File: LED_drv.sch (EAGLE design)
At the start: 46 parts, among them IC1 LM3409, IC2 LM393D, T1 IRLR9343PBF, T4 BT169, T5 BT169, T6 TLP266J

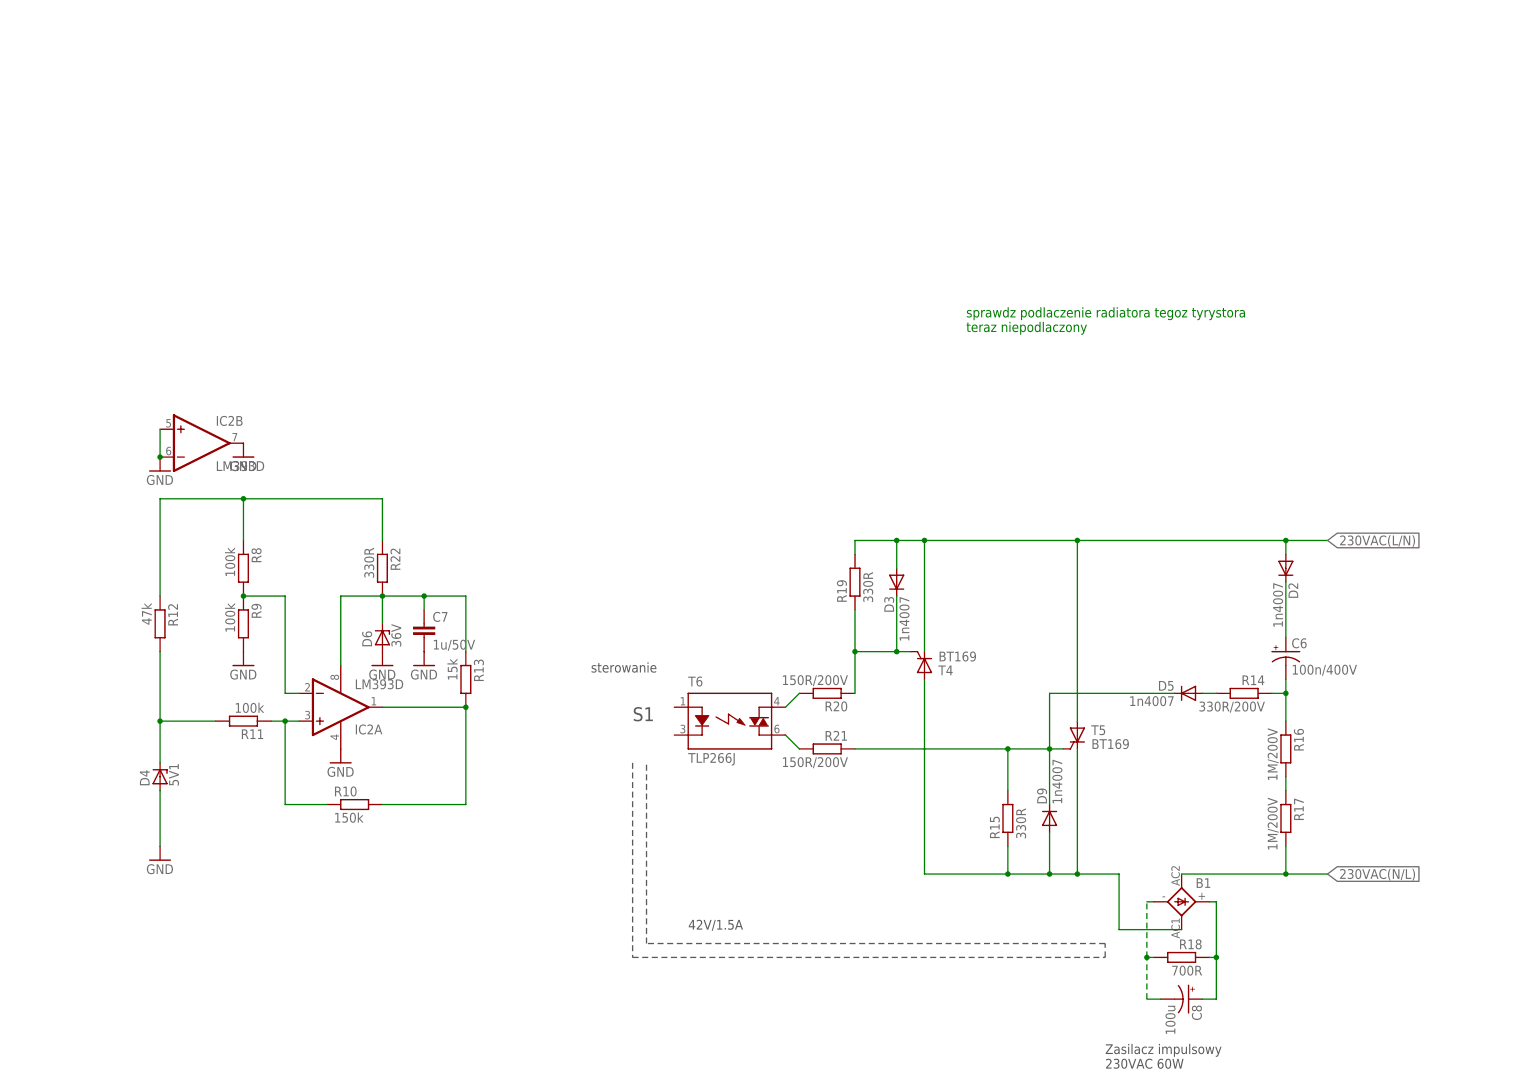
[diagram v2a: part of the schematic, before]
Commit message: Analog circuitry & switch correction
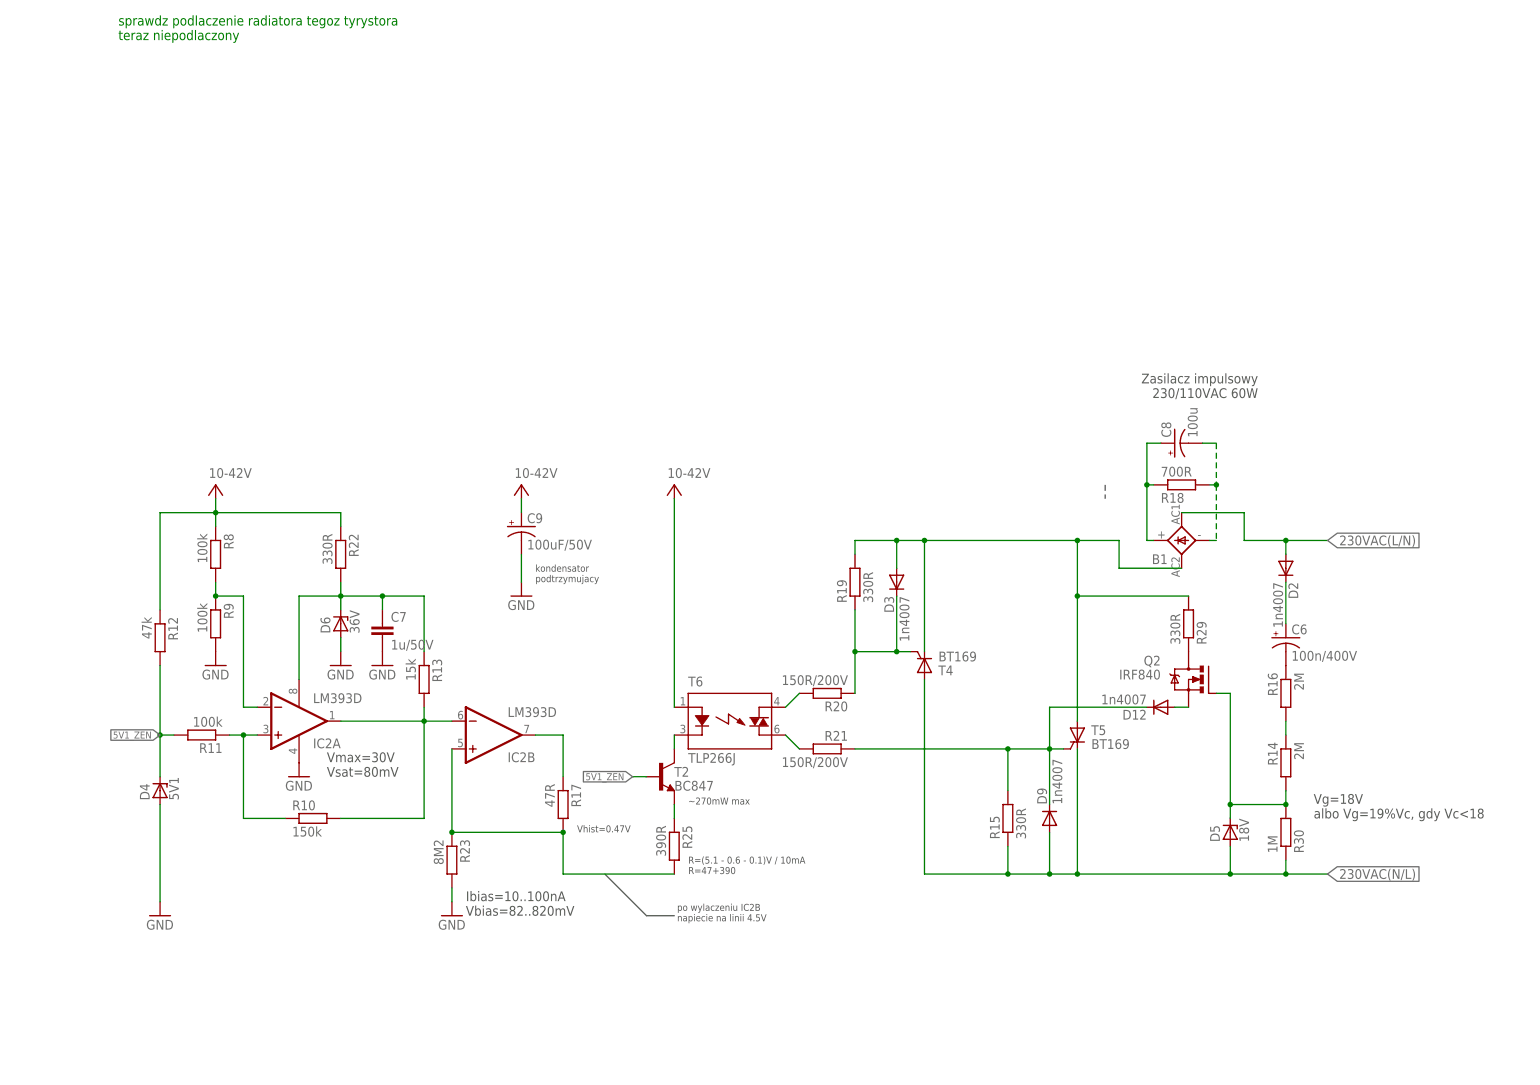
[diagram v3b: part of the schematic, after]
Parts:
- added C9: 100uF/50V, rcl:CPOL-USE3.5-8
- added D12: 1n4007, diode:DIODE-DO-214AC
- added Q2: IRF840, transistor-fet:IRF840
- added R23: 8M2, resistor:R-EU_R0805
- added R25: 390R, resistor:R-EU_R0805
- added R29: 330R, rcl:R-EU_R1206
- added R30: 1M, rcl:R-EU_R1206
- added T2: BC847, transistor:BC847
- D5: value 1n4007 -> 18V; device diode:DIODE-DO-214AC -> diode:ZENER-DIODESOD80C
- R14: value 330R/200V -> 2M
- R16: value 1M/200V -> 2M
- R17: value 1M/200V -> 47R; device rcl:R-EU_R1206 -> resistor:R-EU_R0805
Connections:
- removed net N$24: B1.AC2, D9.A, R15.1, T4.A, T5.C
- new net 5V1_ZEN: D4.C, R11.2, R12.2, T2.B
- new net N$28: IC2B.OUT, R17.1
- new net N$30: IC2B.+IN, R17.2, R23.1, R25.2
- new net N$38: Q2.D, R29.1
- new net N$39: D12.A, Q2.S
- new net NAH: B1.AC1, D3.A, R19.2, R29.2, T4.C, T5.A
- new net V+: C9.+, R12.1, R22.1, R8.1, T6.A
- net 230VAC(L/N): now also B1.AC2; no longer D3.A, R19.2, T4.C, T5.A
- net 230VAC(N/L): now also D5.A, D9.A, R15.1, R30.1, T4.A, T5.C; no longer B1.AC1, R17.2
- net GND: now also C9.-, R23.2; no longer IC2B.+IN, IC2B.-IN, IC2B.OUT
- net N$12: no longer R14.1
- net N$15: now also R14.1, R16.2; no longer D5.A, R14.2
- net N$16: now also D12.C; no longer D5.C
- net N$22: now also R25.1, T2.E; no longer D4.C, R11.2, R12.2
- net N$27: now also T2.C, T6.K; no longer R12.1, R22.1, R8.1
- net N$29: now also IC2B.-IN
- net N$7: now also D5.C, Q2.G, R14.2, R30.2; no longer R16.2, R17.1
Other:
- note added: "Ibias=10..100nA Vbias=82..820mV"
- note added: "R=(5.1 - 0.6 - 0.1)V / 10mA R=47+390"
- note added: "Vg=18V albo Vg=19%Vc, gdy Vc<18"
- note added: "Vhist=0.47V"
- note added: "Vmax=30V Vsat=80mV"
- note added: "Zasilacz impulsowy 230/110VAC 60W"
- note added: "kondensator podtrzymujacy"
- note added: "po wylaczeniu IC2B napiecie na linii 4.5V"
- note added: "~270mW max"
- note removed: "42V/1.5A"
- note removed: "S1"
- note removed: "Zasilacz impulsowy 230VAC 60W"
- note removed: "sterowanie"
- moved on the sheet: B1, C6, C7, C8, D4, D6, IC2A, IC2B, R10, R11, R12, R13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

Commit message: Additional corrections
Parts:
- added R24: 2M2, resistor:R-EU_R0805
- R23: value 8M2 -> 2M2
- T2: value BC847 -> (none); device transistor:BC847 -> transistor:BCX56-NPN-SOT89-BCE
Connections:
- new net N$21: IC2B.+IN, R23.1, R24.1
- net N$30: now also R24.2; no longer IC2B.+IN, R23.1
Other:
- note added: "<450mW on mode"
- note added: "Ibias=10..100nA Vbias=82/4..820/4mV"
- note added: "Vhist=0.47/2V"
- note removed: "Ibias=10..100nA Vbias=82..820mV"
- note removed: "Vhist=0.47V"
- note removed: "~270mW max"
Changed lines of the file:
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@@
 <part name="SUPPLY1" library="supply2" deviceset="V+" device="" value="10-42V"/>
 <part name="GND14" library="supply1" deviceset="GND" device=""/>
-<part name="R23" library="resistor" deviceset="R-EU_" device="R0805" value="8M2"/>
-<part name="T2" library="transistor" deviceset="BC847" device=""/>
+<part name="R23" library="resistor" deviceset="R-EU_" device="R0805" value="2M2"/>
+<part name="T2" library="transistor" deviceset="*-NPN-" device="SOT89-BCE" technology="BCX56"/>
 <part name="R25" library="resistor" deviceset="R-EU_" device="R0805" value="390R"/>
 <part name="SUPPLY3" library="supply2" deviceset="V+" device="" value="10-42V"/>
@@
 <part name="GND15" library="supply1" deviceset="GND" device=""/>
 <part name="C9" library="rcl" deviceset="CPOL-US" device="E3.5-8" value="100uF/50V"/>
+<part name="R24" library="resistor" deviceset="R-EU_" device="R0805" value="2M2"/>
 </parts>
 <sheets>
@@
 Vsat=80mV</text>
 <text x="279.4" y="-45.72" size="1.778" layer="97">Ibias=10..100nA
-Vbias=82..820mV</text>
+Vbias=82/4..820/4mV</text>
 <text x="320.04" y="-38.1" size="1.27" layer="97">R=(5.1 - 0.6 - 0.1)V / 10mA
 R=47+390</text>
-<text x="320.04" y="-25.4" size="1.27" layer="97">~270mW max</text>
-<text x="299.72" y="-30.48" size="1.27" layer="97">Vhist=0.47V</text>
+<text x="320.04" y="-25.4" size="1.27" layer="97">&lt;450mW on mode</text>
+<text x="299.72" y="-30.48" size="1.27" layer="97">Vhist=0.47/2V</text>
 <text x="318.008" y="-46.736" size="1.27" layer="97">po wylaczeniu IC2B
 napiecie na linii 4.5V</text>
@@
 <instance part="GND15" gate="1" x="289.56" y="12.7"/>
 <instance part="C9" gate="G$1" x="289.56" y="25.4"/>
+<instance part="R24" gate="G$1" x="287.02" y="-30.48"/>
 </instances>
 <busses>
@@
 <net name="N$30" class="0">
 <segment>
-<pinref part="IC2" gate="B" pin="+IN"/>
-<pinref part="R23" gate="G$1" pin="1"/>
-<wire x1="276.86" y1="-30.48" x2="276.86" y2="-15.24" width="0.1524" layer="91"/>
 <pinref part="R25" gate="G$1" pin="2"/>
 <wire x1="317.5" y1="-38.1" x2="297.18" y2="-38.1" width="0.1524" layer="91"/>
 <pinref part="R17" gate="G$1" pin="2"/>
 <wire x1="297.18" y1="-30.48" x2="297.18" y2="-38.1" width="0.1524" layer="91"/>
-<wire x1="276.86" y1="-30.48" x2="297.18" y2="-30.48" width="0.1524" layer="91"/>
-<junction x="276.86" y="-30.48"/>
 <junction x="297.18" y="-30.48"/>
+<pinref part="R24" gate="G$1" pin="2"/>
+<wire x1="292.1" y1="-30.48" x2="297.18" y2="-30.48" width="0.1524" layer="91"/>
 </segment>
 </net>
@@
 </segment>
 </net>
+<net name="N$21" class="0">
+<segment>
+<pinref part="IC2" gate="B" pin="+IN"/>
+<pinref part="R24" gate="G$1" pin="1"/>
+<pinref part="R23" gate="G$1" pin="1"/>
+<wire x1="276.86" y1="-30.48" x2="281.94" y2="-30.48" width="0.1524" layer="91"/>
+<junction x="276.86" y="-30.48"/>
+<wire x1="276.86" y1="-30.48" x2="276.86" y2="-15.24" width="0.1524" layer="91"/>
+</segment>
+</net>

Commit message: Mains side PCB layout
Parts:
- removed B1: (no value), rectifier:FBP1,5
- removed C8: 100u, rcl:CPOL-USE3.5-8
- removed D12: 1n4007, diode:DIODE-DO-214AC
- added D7: 1n4007, diode:DIODE-DO-214AC
- added D8: 10V, diode:ZENER-DIODESOD80C
- added PAD1, PAD2, PAD3, PAD4: (no value), wirepad:SMD5
- added R26: 10M, rcl:R-EU_R1206
- Q2: value IRF840 -> IPD50R380; device transistor-fet:IRF840 -> miscrel:IPD50R380
- R18: value 700R -> 10M
- T2: value (none) -> BCX56; device transistor:BCX56-NPN-SOT89-BCE -> miscrel:BCX56
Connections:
- removed net N$17: B1.+, C8.+, R18.1
- removed net N$18: B1.-, C8.-, R18.2
- new net N$24: D7.C, R29.2
- new net N$33: D8.C, Q2.S
- net 230VAC(L/N): now also PAD1.P, PAD4.P; no longer B1.AC2
- net 230VAC(N/L): now also PAD2.P, R26.2
- net N$14: now also R18.1
- net N$16: now also R21.2, T6.DS1; no longer D12.C, D9.C, R15.2, R21.1, T5.G
- net N$25: now also R20.2; no longer R21.2
- net N$26: now also R18.2, R26.1; no longer R20.2, T6.DS1
- net N$39: now also D8.A, D9.C, R15.2, R21.1, T5.G; no longer D12.A, Q2.S
- net NAH: now also D7.A, PAD3.P; no longer B1.AC1, R29.2
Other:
- note added: "3x10M opcjonalnie, kondensator moze się rozladowac przez uplywnosci diod i zasilacz"
- note added: "rezystor bocznikujacy prad uplywnosci diody"
- note added: "zenerka opcjonalnie, by upewnic wylaczenie MOSa"
- moved on the sheet: Q2, R18, R21
